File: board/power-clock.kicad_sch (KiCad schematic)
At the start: 15 parts, among them J3 AdaFruit 4090 USB-C BOB, SW1 RESET, Y4 12MHz

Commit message: update parts I've added
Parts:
- removed J3: AdaFruit 4090 USB-C BOB, Connector_PinHeader_2.54mm:PinHeader_1x08_P2.54mm_Vertical, symbol Connector_Generic:Conn_01x08
- added J13: Barrel_Jack_Switch, symbol Connector:Barrel_Jack_Switch
- Y4: value 12MHz -> SYSCLK
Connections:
- net GND: now also J13.2
- no-connect marks 6 -> 1
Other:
- moved on the sheet: C2

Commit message: checkpoint
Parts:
- removed C1, C3: 10uF, Capacitor_THT:CP_Radial_D5.0mm_P2.50mm, symbol Device:C
- removed J13: Barrel_Jack_Switch, symbol Connector:Barrel_Jack_Switch
- removed R2: 10K, Resistor_THT:R_Axial_DIN0207_L6.3mm_D2.5mm_P10.16mm_Horizontal, symbol Device:R
- removed SW1: RESET, Button_Switch_THT:SW_TH_Tactile_Omron_B3F-106x, symbol Switch:SW_Push
- added CP0: Power Connector, Apple-II:POWER, symbol Connector_Generic:Conn_02x03_Odd_Even
- added D3: 1N5817, Diode_THT:D_DO-41_SOD81_P10.16mm_Horizontal, symbol Diode:1N5817
- added J3: Conn_01x04, symbol Connector_Generic:Conn_01x04
- added R10: 10K, Resistor_THT:R_Axial_DIN0207_L6.3mm_D2.5mm_P10.16mm_Horizontal, symbol Device:R
- added SW2: RESET, Button_Switch_THT:SW_TH_Tactile_Omron_B3F-106x, symbol Switch:SW_Push
- added U14: DS1233, symbol Power_Supervisor:TCM809
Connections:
- net +5V: now also CP0.3 (Pin_3), J3.4 (Pin_4), R10.1, U14.3 (V_{DD})
- net GND: now also CP0.1 (Pin_1), CP0.2 (Pin_2), J3.2 (Pin_2), J3.3 (Pin_3), SW2.1, U14.1 (GND)
- net ~{RESET}: now also D3.2 (A), R10.2
- new net +12V: CP0.4 (Pin_4), J3.1 (Pin_1)
- new net -12V: CP0.5 (Pin_5)
- new net -5V: CP0.6 (Pin_6)
- new net ~{SUPERVISOR_RESET}: D3.1 (K), SW2.2, U14.2 (~{RESET})
- no-connect marks 1 -> 0
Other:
- moved on the sheet: C2, D1, H1, H2, H3, H4, H9, R1, R33, Y4

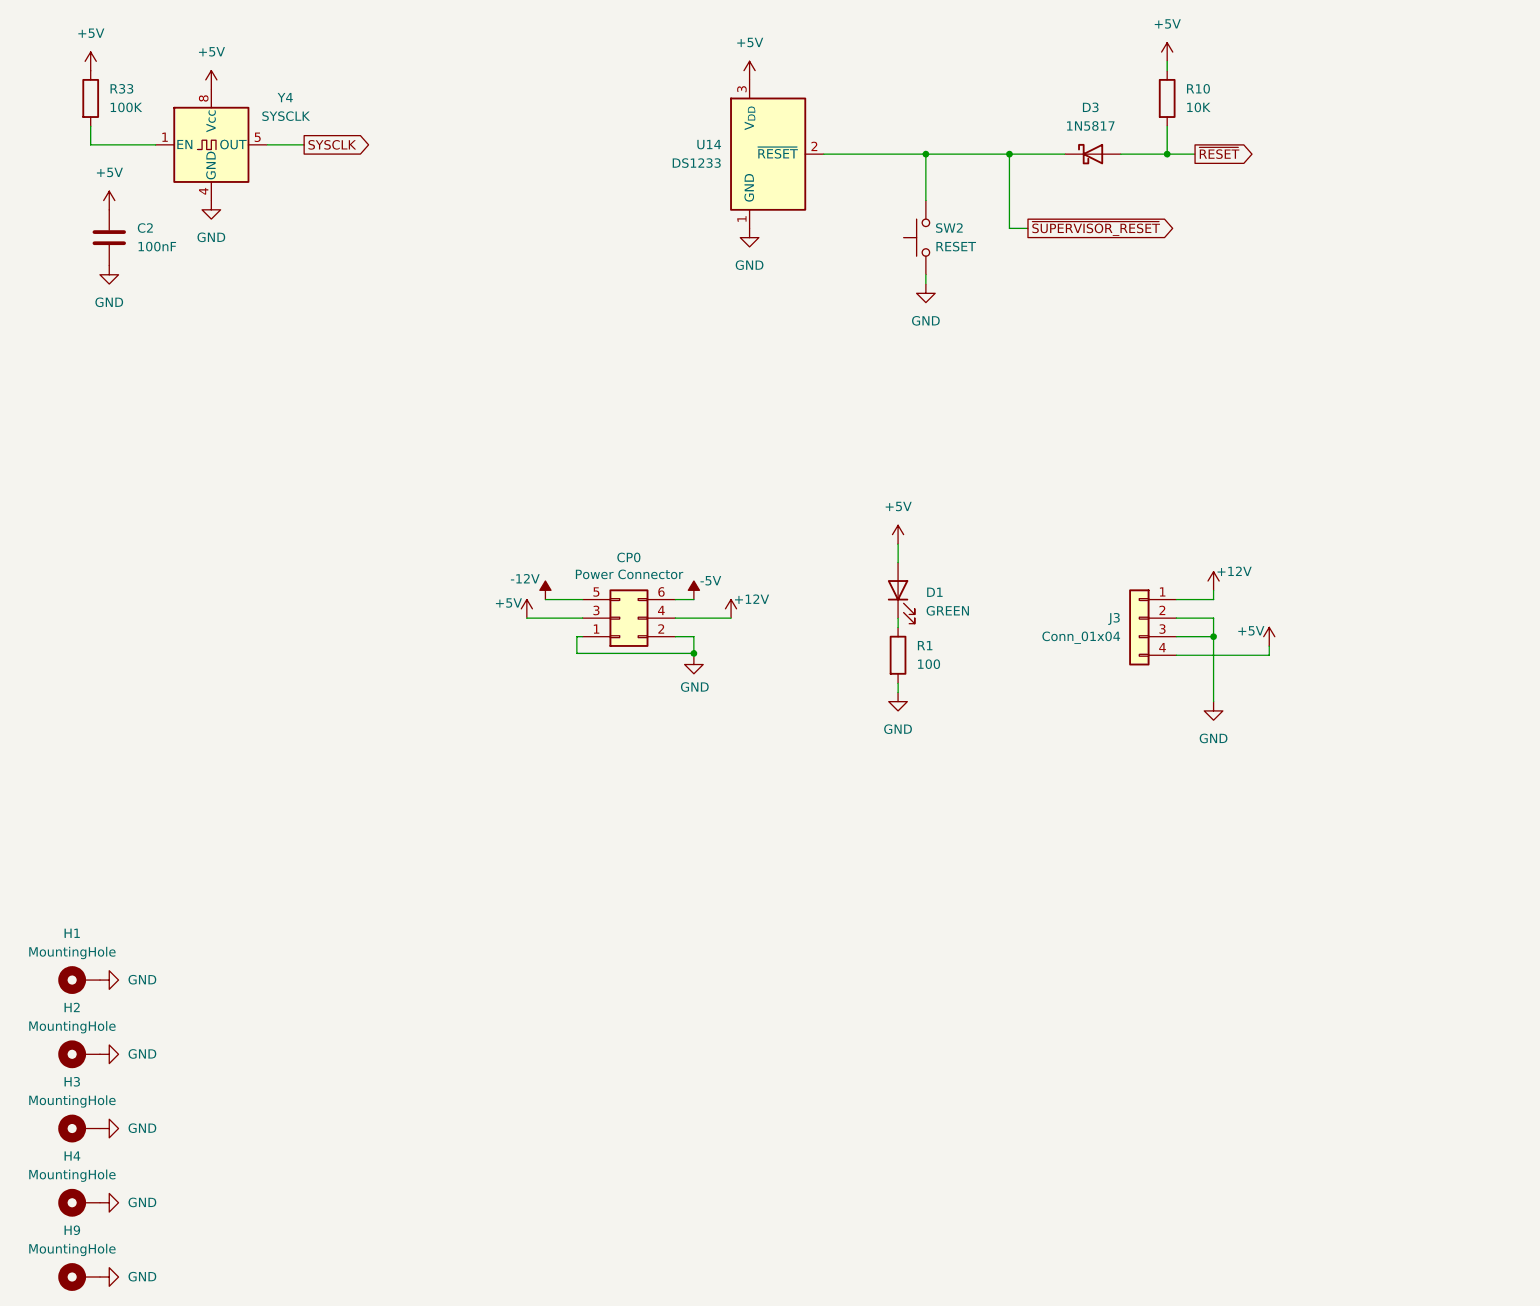
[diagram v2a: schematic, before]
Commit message: capture ENGINE in schematic; fix couple of shorts
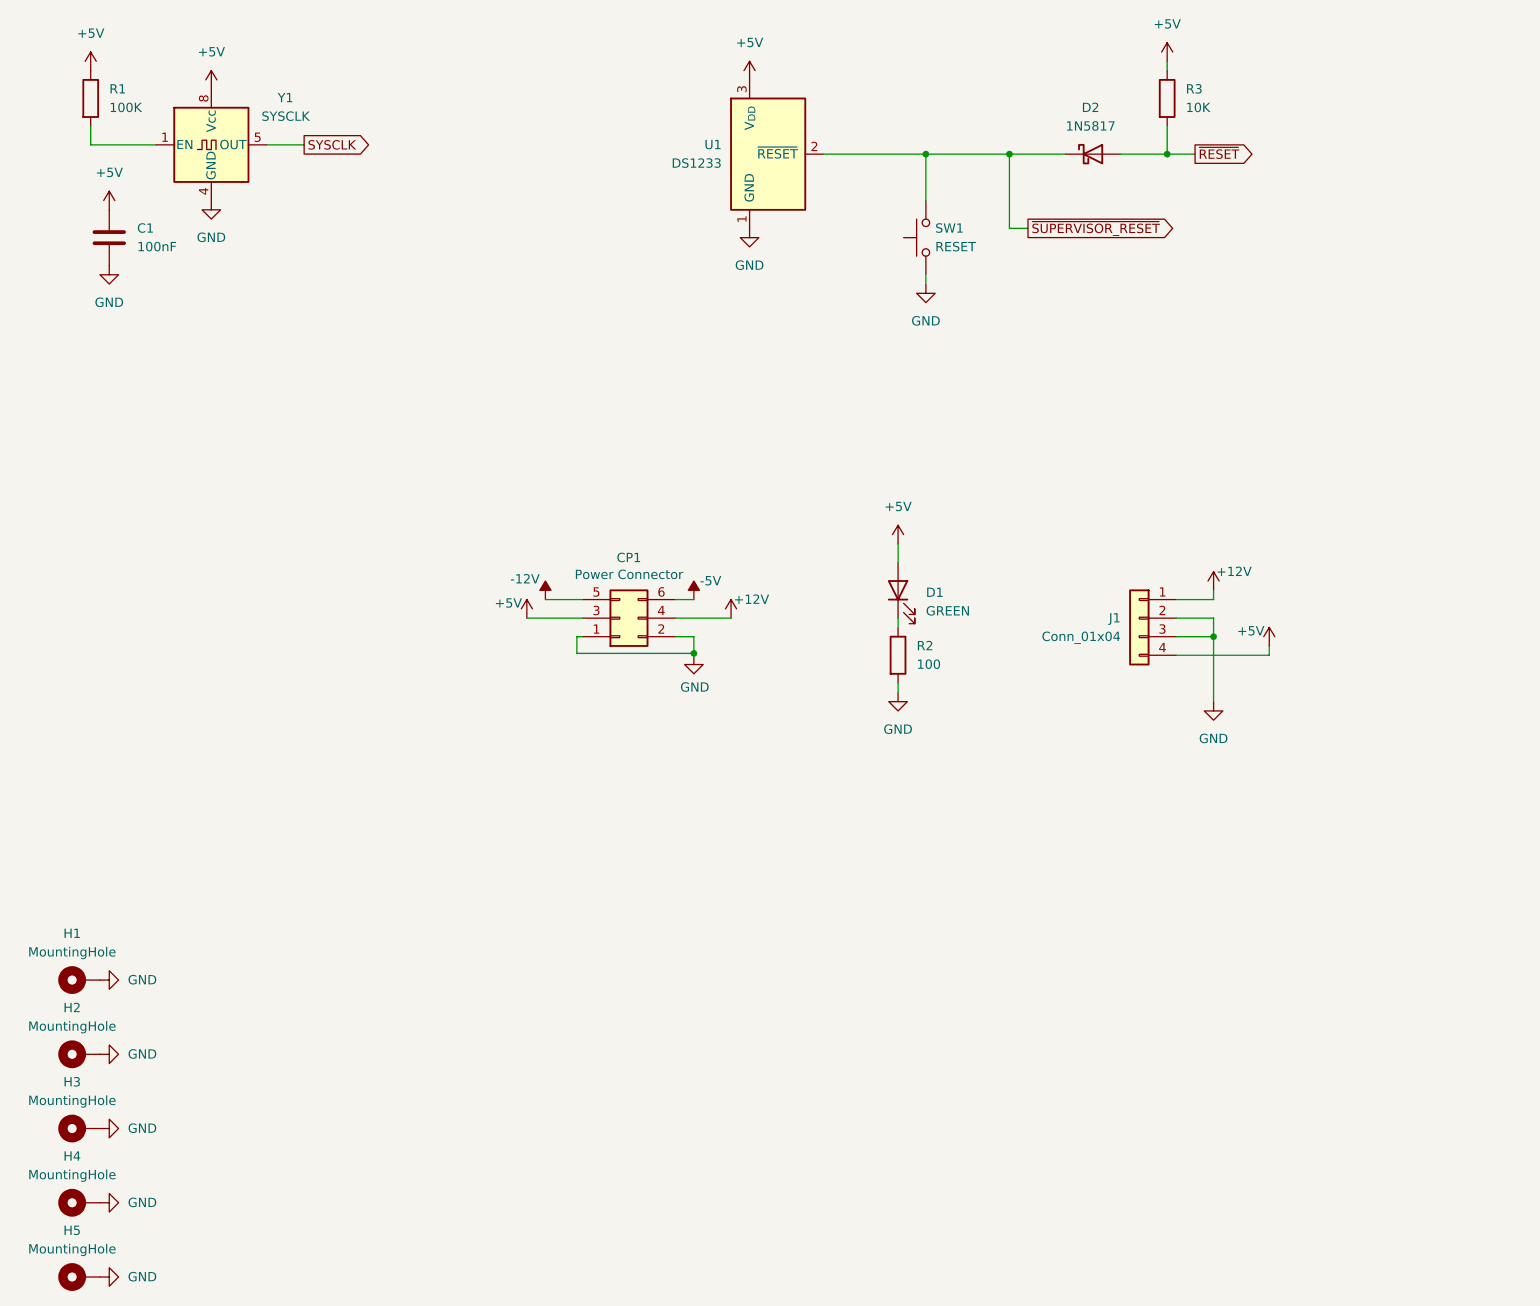
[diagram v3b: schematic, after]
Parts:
- renumbered C2 to C1, CP0 to CP1, D3 to D2, H9 to H5, J3 to J1, R33 to R1, R1 to R2, R10 to R3, SW2 to SW1, U14 to U1, Y4 to Y1
